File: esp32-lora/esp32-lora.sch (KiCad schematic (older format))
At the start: 27 parts

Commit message: Add level translators
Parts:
- added U?: SN74LV1T125, symbol 74lv1t:SN74LV1T125
- added U?: SN74LV4T125, Package_DFN_QFN:Texas_S-PVQFN-N14_ThermalVias, symbol 74lv4t:SN74LV4T125
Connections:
- net labels added: DTR_HV, RTS_HV, RXD_HV, TXD_HV, VUSB
- wire segments 136 -> 147
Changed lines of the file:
@@
 Wire Bus Line
 	3150 1800 4050 1800
+$Comp
+L 74lv1t:SN74LV1T125 U?
+U 1 1 5CC004AA
+P 9150 1550
+F 0 "U?" H 9544 1596 50  0000 L CNN
+F 1 "SN74LV1T125" H 9544 1505 50  0000 L CNN
+F 2 "" H 9150 1550 50  0001 C CNN
+F 3 "" H 9150 1550 50  0001 C CNN
+	1    9150 1550
+	1    0    0    -1
+$EndComp
+$Comp
+L 74lv4t:SN74LV4T125 U?
+U 1 1 5CC1B368
+P 7850 1750
+F 0 "U?" H 7950 2300 50  0000 C CNN
+F 1 "SN74LV4T125" H 7500 2300 50  0000 C CNN
+F 2 "Package_DFN_QFN:Texas_S-PVQFN-N14_ThermalVias" H 7850 1800 50  0001 C CNN
+F 3 "" H 7850 1800 50  0001 C CNN
+	1    7850 1750
+	1    0    0    -1
+$EndComp
+$Comp
+L vusb:VUSB #PWR?
+U 1 1 5CC1C5B6
+P 1950 750
+F 0 "#PWR?" H 1950 600 50  0001 C CNN
+F 1 "VUSB" H 1932 923 50  0000 C CNN
+F 2 "" H 1950 750 50  0001 C CNN
+F 3 "" H 1950 750 50  0001 C CNN
+	1    1950 750
+	1    0    0    -1
+$EndComp
+Wire Wire Line
+	1950 950  1950 750
+Text Label 6050 1500 0    50   ~ 0
+RTS_HV
+Text Label 6050 1600 0    50   ~ 0
+RXD_HV
+Text Label 6050 1700 0    50   ~ 0
+TXD_HV
+Text Label 6050 1900 0    50   ~ 0
+DTR_HV
+Wire Wire Line
+	6000 1500 6400 1500
+Wire Wire Line
+	6000 1600 6400 1600
+Wire Wire Line
+	6000 1700 6400 1700
+Wire Wire Line
+	6000 1900 6400 1900
+Entry Wire Line
+	6400 1500 6500 1600
+Entry Wire Line
+	6400 1600 6500 1700
+Entry Wire Line
+	6400 1700 6500 1800
+Entry Wire Line
+	6400 1900 6500 2000
+$Comp
+L power:VDD #PWR?
+U 1 1 5CC40619
+P 7850 1050
+F 0 "#PWR?" H 7850 900 50  0001 C CNN
+F 1 "VDD" H 7867 1223 50  0000 C CNN
+F 2 "" H 7850 1050 50  0001 C CNN
+F 3 "" H 7850 1050 50  0001 C CNN
+	1    7850 1050
+	1    0    0    -1
+$EndComp
+Wire Wire Line
+	7850 1050 7850 1150
+Wire Wire Line
+	7850 2400 7850 2800
+Wire Wire Line
+	5500 2800 5700 2800
+Connection ~ 5500 2800
+Connection ~ 5700 2800
+Wire Wire Line
+	5700 2800 5800 2800
+Connection ~ 5800 2800
+Wire Wire Line
+	5800 2800 7850 2800
+$Comp
+L vusb:VUSB #PWR?
+U 1 1 5CC619E9
+P 9150 1050
+F 0 "#PWR?" H 9150 900 50  0001 C CNN
+F 1 "VUSB" H 9132 1223 50  0000 C CNN
+F 2 "" H 9150 1050 50  0001 C CNN
+F 3 "" H 9150 1050 50  0001 C CNN
+	1    9150 1050
+	1    0    0    -1
+$EndComp
+Wire Wire Line
+	9150 1050 9150 1200
 Wire Wire Line
 	3700 2200 4800 2200

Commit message: Add manual control buttons
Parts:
- removed U?: SN74LV1T125, symbol 74lv1t:SN74LV1T125
- removed U?: SN74LV4T125, Package_DFN_QFN:Texas_S-PVQFN-N14_ThermalVias, symbol 74lv4t:SN74LV4T125
- added D?: D, symbol Device:D
- added Q? (x2): FDG6335N, Package_TO_SOT_SMD:SOT-363_SC-70-6, symbol Transistor_FET:FDG6335N
- added Q?: PMV32UP, Package_TO_SOT_SMD:SOT-23, symbol pmv32up:PMV32UP
- added R? (x2): 10 kR, symbol Device:R
- added R? (x3): 100 kR, symbol Device:R
- added R? (x2): 1 kR, symbol Device:R
- added SW? (x2): SW_Push, symbol Switch:SW_Push
- added U? (x2): SN74LV1T125, Package_TO_SOT_SMD:SOT-23-5, symbol 74lv1t:SN74LV1T125
- U?: symbol espressif-xess:ESP32 -> esp32-lora-rescue:ESP32-espressif-xess
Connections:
- net labels added: CHIP_PU, GPIO0, GPIO0_BOOT, RXD_LV, TXD_LV, UART_LV
- wire segments 147 -> 200
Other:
- note added: "BOOTLOADER"
- note added: "RESET"
- note added: "UART HV"
- moved on the sheet: BT?, C?, L?, Q?, R?, U?

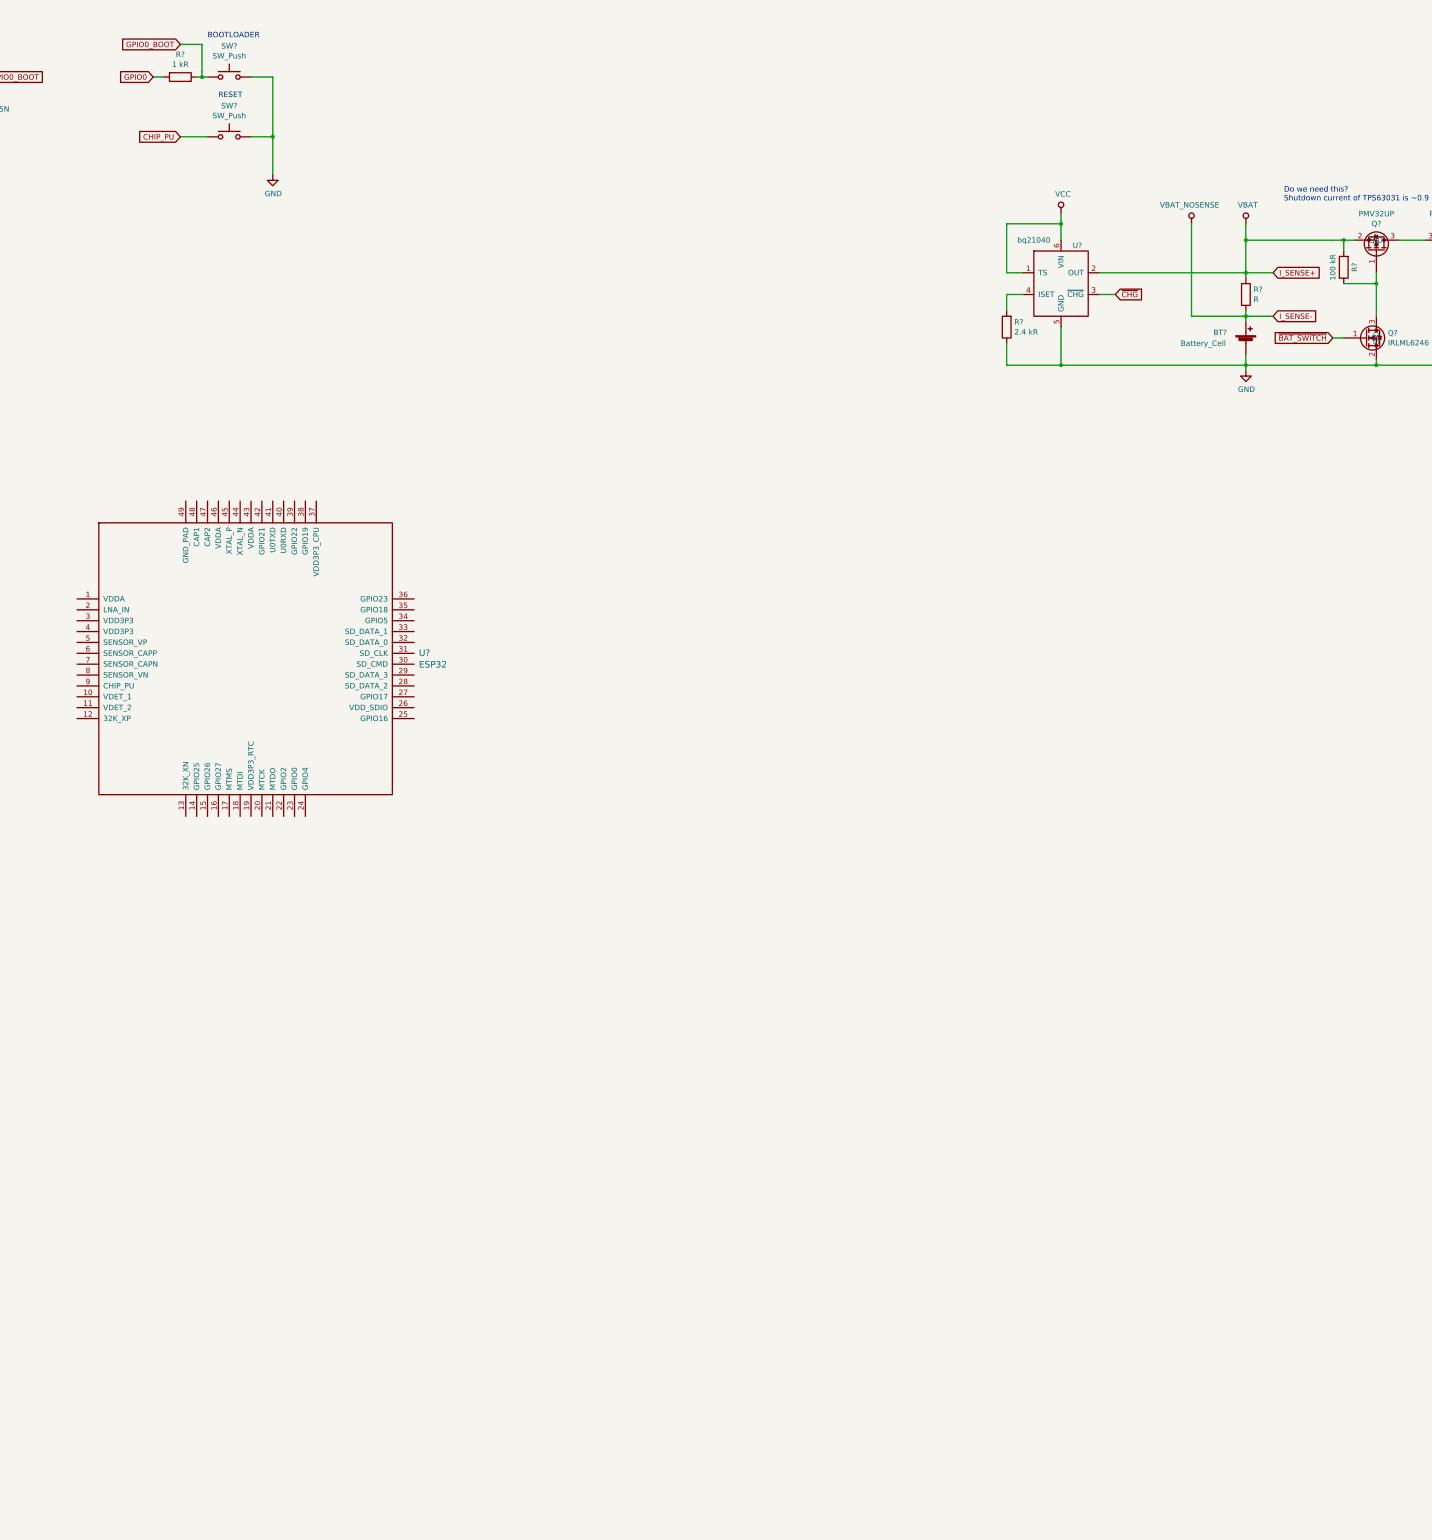
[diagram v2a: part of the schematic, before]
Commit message: Wire ESP32
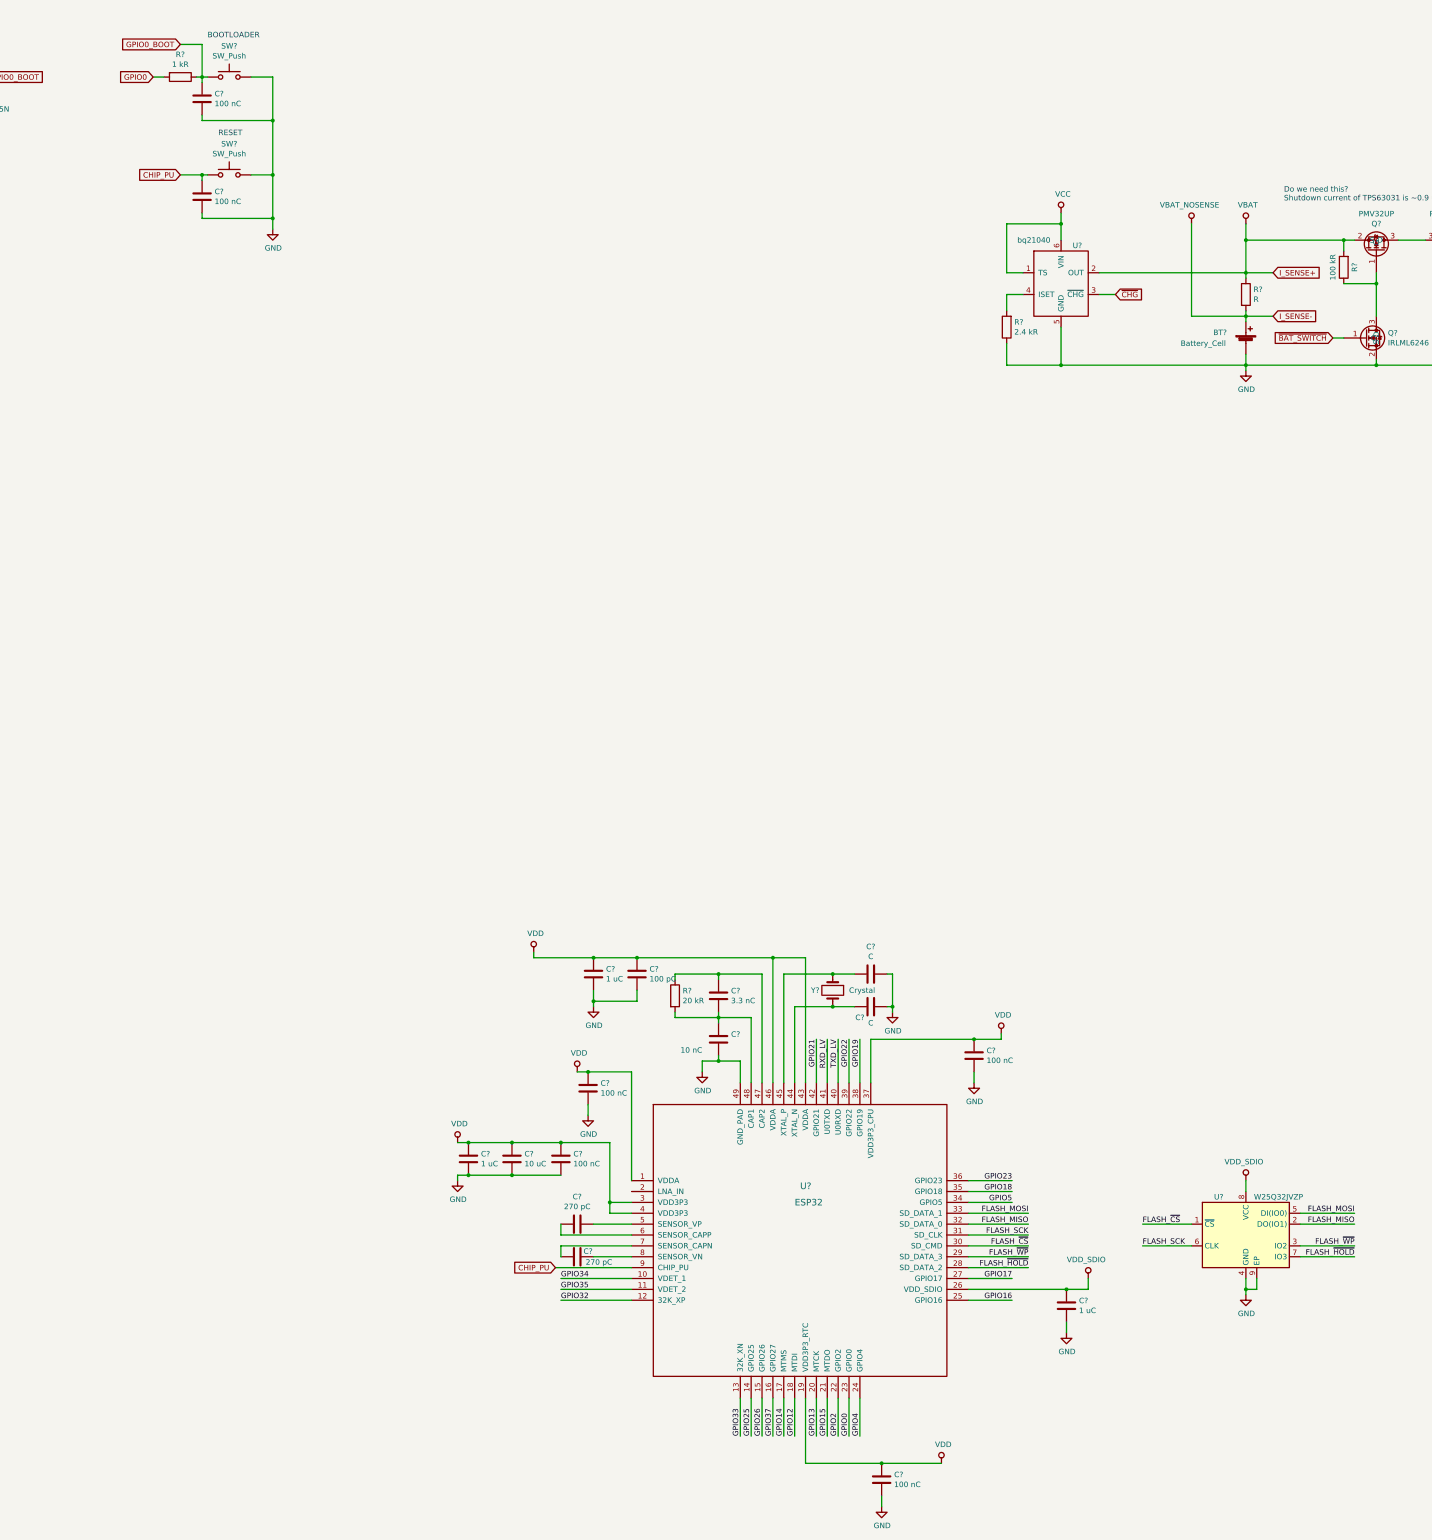
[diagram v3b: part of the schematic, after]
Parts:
- added C? (x6): 100 nC, symbol Device:C
- added C?: 10 uC, symbol Device:C
- added C? (x3): 1 uC, symbol Device:C
- added C? (x2): 270 pC, symbol Device:C
- added C?: 10 nC, symbol Device:C
- added C?: 3.3 nC, symbol Device:C
- added C?: 100 pC, symbol Device:C
- added C? (x2): C, symbol Device:C
- added R?: 20 kR, symbol Device:R
- added U?: W25Q32JVZP, Package_SON:WSON-8-1EP_6x5mm_P1.27mm_EP3.4x4.3mm, symbol Memory_Flash:W25Q32JVZP
- added Y?: Crystal, symbol Device:Crystal
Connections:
- net CHIP_PU: now also U?.9 (CHIP_PU), C?.1
- net GND: now also U?.49 (GND_PAD), C?.1, C?.2, C?.2, C?.2, C?.2, C?.2, C?.2, C?.2, C?.2, C?.2, C?.2, C?.2, C?.2, C?.2, U?.4 (GND), U?.9 (EP)
- net GPIO0: now also U?.23 (GPIO0)
- net GPIO0_BOOT: now also C?.1
- net RXD_LV: now also U?.41 (U0TXD)
- net TXD_LV: now also U?.40 (U0RXD)
- net VDD: now also U?.1 (VDDA), U?.19 (VDD3P3_RTC), U?.3 (VDD3P3), U?.37 (VDD3P3_CPU), U?.4 (VDD3P3), U?.43 (VDDA), U?.46 (VDDA), C?.1, C?.1, C?.1, C?.1, C?.1, C?.1, C?.1, C?.1
- net GPIO34: now reaches U?.10 (VDET_1)
- net GPIO35: now reaches U?.11 (VDET_2)
- net GPIO32: now reaches U?.12 (32K_XP)
- net GPIO33: now reaches U?.13 (32K_XN)
- net GPIO25: now reaches U?.14 (GPIO25)
- net GPIO26: now reaches U?.15 (GPIO26)
- net GPIO37: now reaches U?.16 (GPIO27)
- net GPIO14: now reaches U?.17 (MTMS)
- net GPIO12: now reaches U?.18 (MTDI)
- net GPIO13: now reaches U?.20 (MTCK)
- net GPIO15: now reaches U?.21 (MTDO)
- net GPIO2: now reaches U?.22 (GPIO2)
- net GPIO4: now reaches U?.24 (GPIO4)
- net GPIO16: now reaches U?.25 (GPIO16)
- net VDD_SDIO: now reaches U?.26 (VDD_SDIO)
- net VDD_SDIO: now also C?.1, U?.8 (VCC)
- net GPIO17: now reaches U?.27 (GPIO17)
- net FLASH_~HOLD: now reaches U?.28 (SD_DATA_2)
- net FLASH_~HOLD: now also U?.7 (IO3)
- net FLASH_~WP: now reaches U?.29 (SD_DATA_3)
- net FLASH_~WP: now also U?.3 (IO2)
- net FLASH_~CS: now reaches U?.30 (SD_CMD)
- net FLASH_~CS: now also U?.1 (~CS)
- net FLASH_SCK: now reaches U?.31 (SD_CLK)
- net FLASH_SCK: now also U?.6 (CLK)
- net FLASH_MISO: now reaches U?.32 (SD_DATA_0)
- net FLASH_MISO: now also U?.2 (DO(IO1))
- net FLASH_MOSI: now reaches U?.33 (SD_DATA_1)
- net FLASH_MOSI: now also U?.5 (DI(IO0))
- net GPIO5: now reaches U?.34 (GPIO5)
- net GPIO18: now reaches U?.35 (GPIO18)
- net GPIO23: now reaches U?.36 (GPIO23)
- net GPIO19: now reaches U?.38 (GPIO19)
- net GPIO22: now reaches U?.39 (GPIO22)
- net GPIO21: now reaches U?.42 (GPIO21)
- net at U?.44 (XTAL_N): now also C?.1, Y?.2
- net at U?.45 (XTAL_P): now also C?.2, Y?.1
- net at U?.47 (CAP2): now also C?.1, R?.1
- net at U?.48 (CAP1): now also C?.1, C?.2, R?.2
- net at U?.5 (SENSOR_VP): now also C?.1
- net at U?.6 (SENSOR_CAPP): now also C?.2
- net at U?.7 (SENSOR_CAPN): now also C?.2
- net at U?.8 (SENSOR_VN): now also C?.1
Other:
- moved on the sheet: SW?, U?
